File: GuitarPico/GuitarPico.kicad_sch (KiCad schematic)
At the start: 112 parts, among them J1 INPUT, J2 INPUT, J3 OUTPUT, J4 OUTPUT, J5 Barrel_Jack_Switch, J6 INPUT, J7 INPUT, J8 INPUT, J9 INPUT, Q1 2N3904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

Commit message: Before replacing with buttons
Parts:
- added C30: 100 pF, Capacitor_THT:C_Disc_D5.0mm_W2.5mm_P5.00mm, symbol Device:C_Small
- C12: value 330 nF -> 220 pF
- C13: value 2200 pF -> 220 pF
- R13, R14, R15: value 1k -> 10k
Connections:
- net CTRLIN: now also C30.1
- net GND: now also C30.2
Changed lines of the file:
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@@
   (junction (at 283.21 77.47) (diameter 0) (color 0 0 0 0)
   )
+  (junction (at 279.4 115.57) (diameter 0) (color 0 0 0 0)
+  )
   (junction (at 76.2 92.075) (diameter 0) (color 0 0 0 0)
   )
@@
     (stroke (width 0) (type default) (color 0 0 0 0))
   )
+  (wire (pts (xy 276.86 115.57) (xy 279.4 115.57))
+    (stroke (width 0) (type default) (color 0 0 0 0))
+  )
   (wire (pts (xy 110.49 103.505) (xy 101.6 103.505))
     (stroke (width 0) (type default) (color 0 0 0 0))
   )
+  (wire (pts (xy 279.4 115.57) (xy 279.4 114.935))
+    (stroke (width 0) (type default) (color 0 0 0 0))
+  )
   (wire (pts (xy 84.455 185.42) (xy 84.455 186.69))
     (stroke (width 0) (type default) (color 0 0 0 0))
@@
     (stroke (width 0) (type default) (color 0 0 0 0))
   )
+  (wire (pts (xy 279.4 116.205) (xy 279.4 115.57))
+    (stroke (width 0) (type default) (color 0 0 0 0))
+  )
   (wire (pts (xy 52.07 180.975) (xy 52.07 180.34))
     (stroke (width 0) (type default) (color 0 0 0 0))
@@
     (stroke (width 0) (type default) (color 0 0 0 0))
   )
+  (wire (pts (xy 276.86 132.08) (xy 276.86 133.985))
+    (stroke (width 0) (type default) (color 0 0 0 0))
+  )
   (wire (pts (xy 269.875 41.275) (xy 269.875 42.545))
     (stroke (width 0) (type default) (color 0 0 0 0))
@@
     (stroke (width 0) (type default) (color 0 0 0 0))
   )
+  (wire (pts (xy 276.86 115.57) (xy 276.86 127))
+    (stroke (width 0) (type default) (color 0 0 0 0))
+  )
   (wire (pts (xy 265.43 38.735) (xy 265.43 42.545))
     (stroke (width 0) (type default) (color 0 0 0 0))
@@
     )
   )
-  (global_label "CTRLIN" (shape input) (at 279.4 114.935 270) (fields_autoplaced)
+  (global_label "CTRLIN" (shape input) (at 279.4 116.205 270) (fields_autoplaced)
     (effects (font (size 1.27 1.27)) (justify right))
-    (property "Intersheet References" "${INTERSHEET_REFS}" (id 0) (at 279.4794 123.8191 90)
+    (property "Intersheet References" "${INTERSHEET_REFS}" (id 0) (at 279.4794 125.0891 90)
       (effects (font (size 1.27 1.27)) (justify right) hide)
     )
@@
     (pin "2")
   )
+  (symbol (lib_id "Device:C_Small") (at 276.86 129.54 0) (unit 1)
+    (in_bom yes) (on_board yes)
+    (property "Reference" "C30" (id 0) (at 280.67 130.81 0)
+      (effects (font (size 1.27 1.27)) (justify right))
+    )
+    (property "Value" "100 pF" (id 1) (at 284.48 127.635 0)
+      (effects (font (size 1.27 1.27)) (justify right))
+    )
+    (property "Footprint" "Capacitor_THT:C_Disc_D5.0mm_W2.5mm_P5.00mm" (id 2) (at 276.86 129.54 0)
+      (effects (font (size 1.27 1.27)) hide)
+    )
+    (property "Datasheet" "~" (id 3) (at 276.86 129.54 0)
+      (effects (font (size 1.27 1.27)) hide)
+    )
+    (pin "1")
+    (pin "2")
+  )
   (symbol (lib_id "Device:C_Small") (at 123.317 43.561 270) (unit 1)
     (in_bom yes) (on_board yes)
@@
       (effects (font (size 1.27 1.27)) (justify left))
     )
-    (property "Value" "1k" (id 1) (at 42.545 82.55 90)
+    (property "Value" "10k" (id 1) (at 42.545 82.55 90)
       (effects (font (size 1.27 1.27)) (justify left))
     )
@@
       (effects (font (size 1.27 1.27)) (justify left))
     )
-    (property "Value" "1k" (id 1) (at 54.61 82.55 90)
+    (property "Value" "10k" (id 1) (at 54.61 82.55 90)
       (effects (font (size 1.27 1.27)) (justify left))
     )
@@
       (effects (font (size 1.27 1.27)) (justify left))
     )
-    (property "Value" "330 nF" (id 1) (at 49.53 78.7462 0)
+    (property "Value" "220 pF" (id 1) (at 49.53 78.7462 0)
       (effects (font (size 1.27 1.27)) (justify left))
     )
@@
     (pin "2")
   )
+  (symbol (lib_id "power:GND") (at 276.86 133.985 0) (unit 1)
+    (in_bom yes) (on_board yes) (fields_autoplaced)
+    (property "Reference" "#PWR0154" (id 0) (at 276.86 140.335 0)
+      (effects (font (size 1.27 1.27)) hide)
+    )
+    (property "Value" "GND" (id 1) (at 276.86 138.43 0))
+    (property "Footprint" "" (id 2) (at 276.86 133.985 0)
+      (effects (font (size 1.27 1.27)) hide)
+    )
+    (property "Datasheet" "" (id 3) (at 276.86 133.985 0)
+      (effects (font (size 1.27 1.27)) hide)
+    )
+    (pin "1")
+  )
   (symbol (lib_id "power:+5V") (at 276.225 21.59 0) (unit 1)
     (in_bom yes) (on_board yes) (fields_autoplaced)
@@
       (effects (font (size 1.27 1.27)) (justify left))
     )
-    (property "Value" "1k" (id 1) (at 69.215 99.06 90)
+    (property "Value" "10k" (id 1) (at 69.215 99.06 90)
       (effects (font (size 1.27 1.27)) (justify left))
     )
@@
     (in_bom yes) (on_board yes)
     (property "Reference" "C13" (id 0) (at 67.945 88.9 90))
-    (property "Value" "2200 pF" (id 1) (at 67.945 95.25 90))
+    (property "Value" "220 pF" (id 1) (at 67.945 95.25 90))
     (property "Footprint" "Capacitor_THT:C_Disc_D5.0mm_W2.5mm_P5.00mm" (id 2) (at 67.945 92.075 0)
       (effects (font (size 1.27 1.27)) hide)
@@
       (reference "#PWR0153") (unit 1) (value "GND") (footprint "")
     )
+    (path "/c9b51cd9-edc6-4038-85ec-d1dec8977489"
+      (reference "#PWR0154") (unit 1) (value "GND") (footprint "")
+    )
     (path "/eeed5017-d7ea-4c03-bcf7-e3cc8a7830ea"
       (reference "Brd1") (unit 1) (value "SSD1306") (footprint "GuitarPico:128x64OLED")
@@
     )
     (path "/944a30cb-00bd-425f-b8d2-7613a7bc143d"
-      (reference "C12") (unit 1) (value "330 nF") (footprint "Capacitor_THT:C_Disc_D5.0mm_W2.5mm_P5.00mm")
+      (reference "C12") (unit 1) (value "220 pF") (footprint "Capacitor_THT:C_Disc_D5.0mm_W2.5mm_P5.00mm")
     )
     (path "/f9e582af-f7a7-46da-b838-4d87800ad119"
-      (reference "C13") (unit 1) (value "2200 pF") (footprint "Capacitor_THT:C_Disc_D5.0mm_W2.5mm_P5.00mm")
+      (reference "C13") (unit 1) (value "220 pF") (footprint "Capacitor_THT:C_Disc_D5.0mm_W2.5mm_P5.00mm")
     )
     (path "/7b62232e-dc1b-424a-bd96-df5531b112a2"
@@
       (reference "C29") (unit 1) (value "100 nF") (footprint "Capacitor_THT:C_Disc_D5.0mm_W2.5mm_P5.00mm")
     )
+    (path "/1c3bfbaf-43b7-4fed-90fb-53769c1c1fb4"
+      (reference "C30") (unit 1) (value "100 pF") (footprint "Capacitor_THT:C_Disc_D5.0mm_W2.5mm_P5.00mm")
+    )
     (path "/c47f2778-675e-4a19-8402-9385e9308b9c"
       (reference "D1") (unit 1) (value "1N5819") (footprint "Diode_THT:D_DO-41_SOD81_P7.62mm_Horizontal")
@@
     )
     (path "/497e8e16-db24-4b63-b1a9-654c978540b6"
-      (reference "R13") (unit 1) (value "1k") (footprint "Resistor_THT:R_Axial_DIN0207_L6.3mm_D2.5mm_P7.62mm_Horizontal")
+      (reference "R13") (unit 1) (value "10k") (footprint "Resistor_THT:R_Axial_DIN0207_L6.3mm_D2.5mm_P7.62mm_Horizontal")
     )
     (path "/8311fdd2-488f-44b2-97f8-bec3fa3e522a"
-      (reference "R14") (unit 1) (value "1k") (footprint "Resistor_THT:R_Axial_DIN0207_L6.3mm_D2.5mm_P7.62mm_Horizontal")
+      (reference "R14") (unit 1) (value "10k") (footprint "Resistor_THT:R_Axial_DIN0207_L6.3mm_D2.5mm_P7.62mm_Horizontal")
     )
     (path "/dee588ca-cd6f-49bd-8482-b92f631940ad"
-      (reference "R15") (unit 1) (value "1k") (footprint "Resistor_THT:R_Axial_DIN0207_L6.3mm_D2.5mm_P7.62mm_Horizontal")
+      (reference "R15") (unit 1) (value "10k") (footprint "Resistor_THT:R_Axial_DIN0207_L6.3mm_D2.5mm_P7.62mm_Horizontal")
     )
     (path "/f985247c-ef50-4b7d-a7ba-9d9ed0bb0d70"

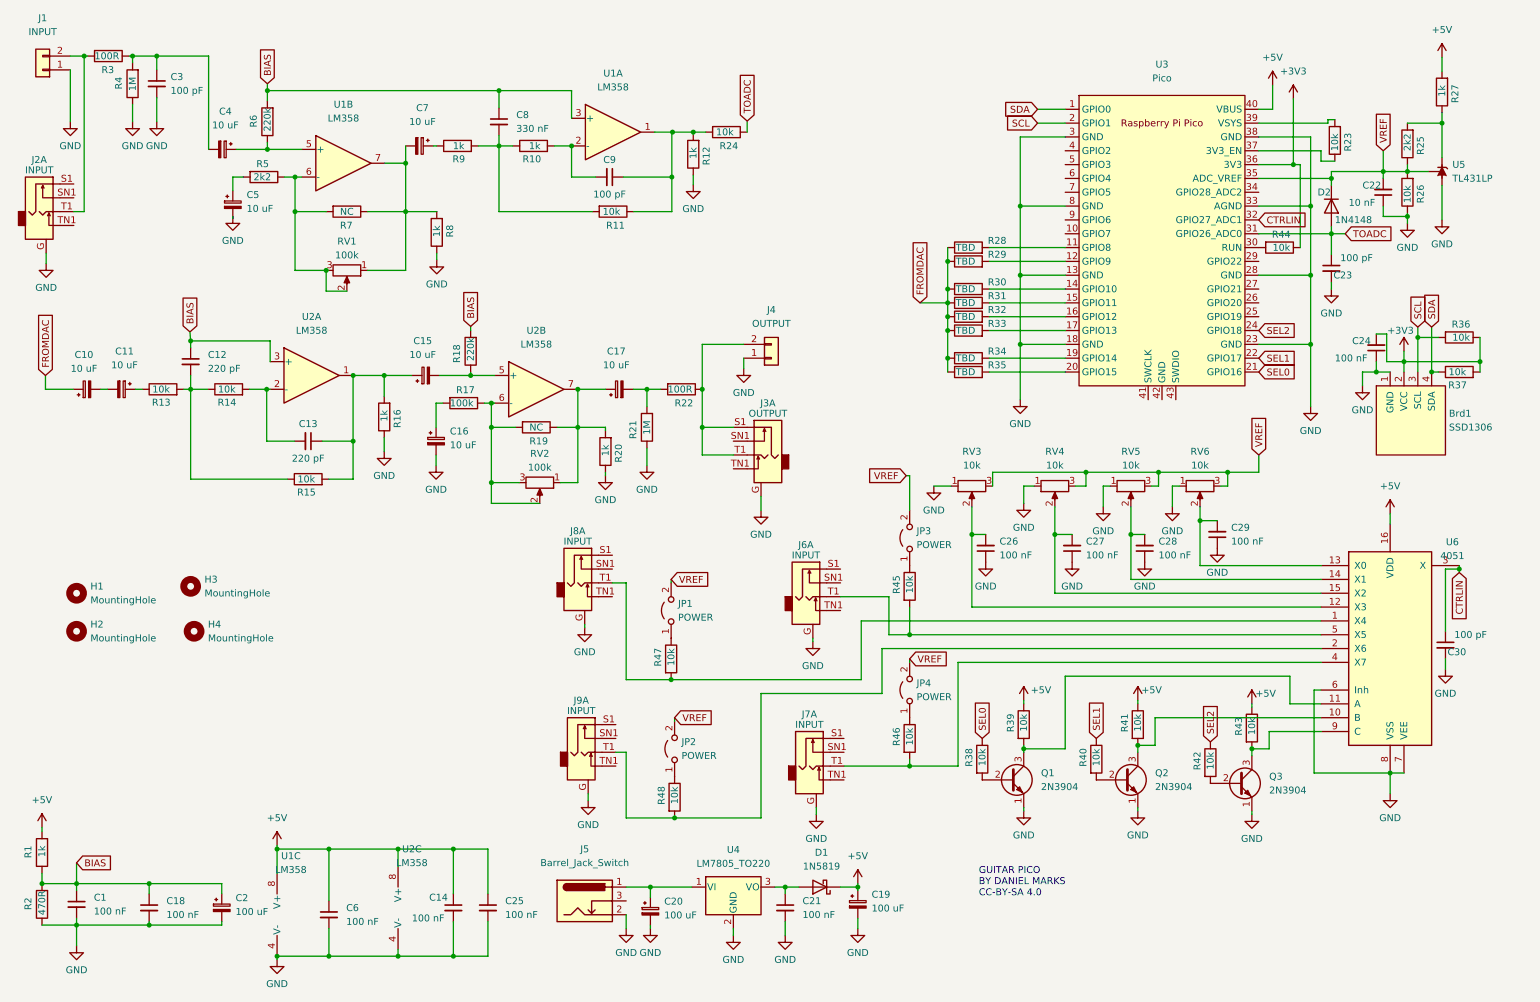
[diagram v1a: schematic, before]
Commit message: replaced with buttons
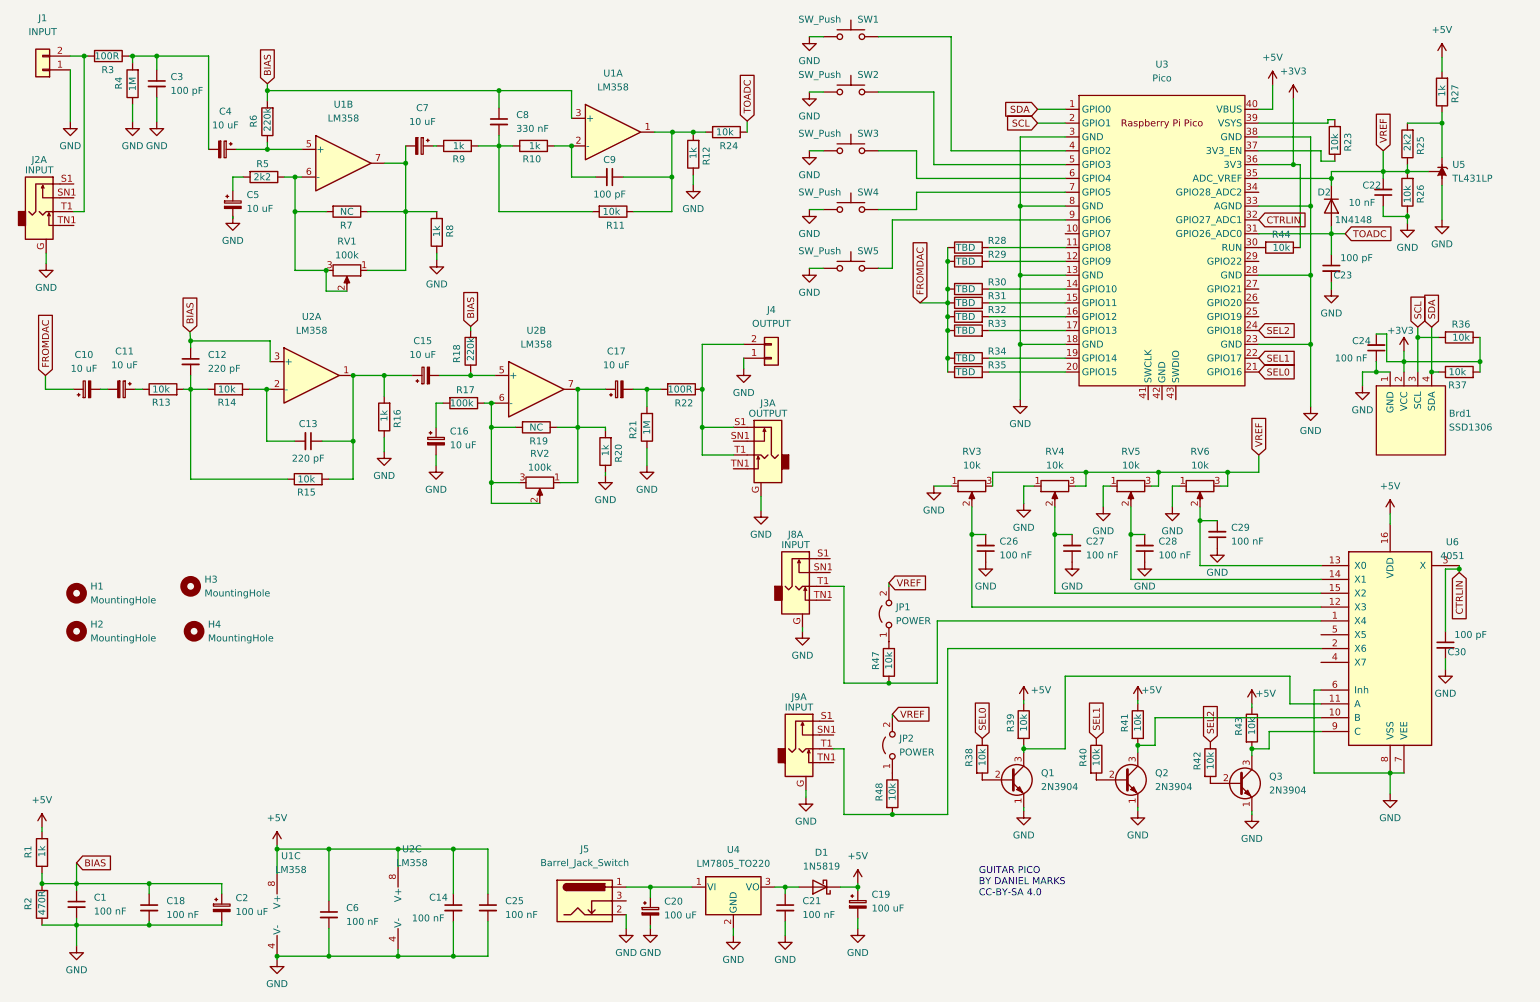
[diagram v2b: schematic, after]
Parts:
- removed J6, J7: INPUT, GuitarPico:PJ-3240-35mm-stereo, symbol Connector:AudioJack2_Dual_Ground_Switch
- removed JP3, JP4: POWER, Connector_PinHeader_2.54mm:PinHeader_1x02_P2.54mm_Vertical, symbol Jumper:Jumper_2_Open
- removed R45, R46: 10k, Resistor_THT:R_Axial_DIN0207_L6.3mm_D2.5mm_P7.62mm_Horizontal, symbol Device:R
- added SW1, SW2, SW3, SW4, SW5: SW_Push, Button_Switch_THT:SW_PUSH_6mm, symbol Switch:SW_Push
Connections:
- net GND: now also SW1.1, SW2.1, SW3.1, SW4.1, SW5.1
- net at U3.4 (GPIO2): now also SW1.2
- net at U3.5 (GPIO3): now also SW2.2
- net at U3.6 (GPIO4): now also SW3.2
- net at U3.7 (GPIO5): now also SW4.2
- net at U3.9 (GPIO6): now also SW5.2
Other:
- moved on the sheet: J8A, J9A, JP1, JP2, R47, R48

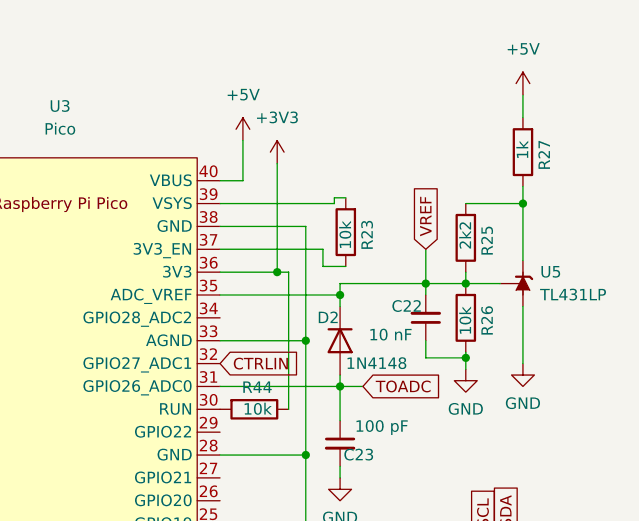
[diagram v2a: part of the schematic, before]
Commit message: Fixed TL431 wiring problem
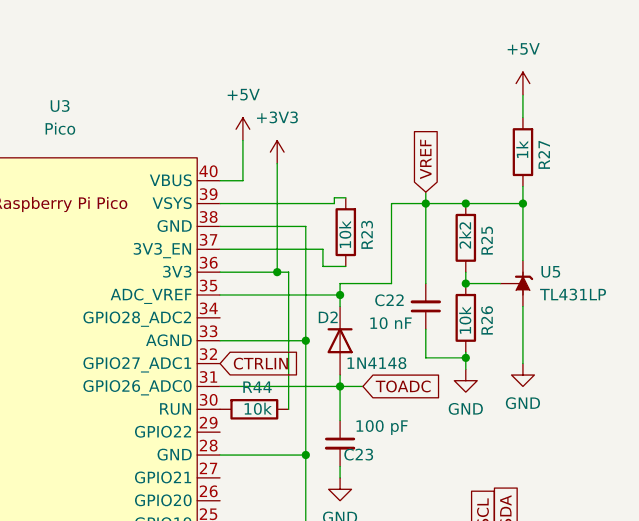
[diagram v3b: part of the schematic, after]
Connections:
- net VREF: now also R25.2, R27.1, U5.3 (K); no longer R25.1, R26.2, U5.1 (REF)
- new net: R25.1, R26.2, U5.1 (REF)
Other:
- moved on the sheet: C22
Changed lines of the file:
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@@
   (junction (at 224.155 97.79) (diameter 0) (color 0 0 0 0)
   )
+  (junction (at 265.43 33.655) (diameter 0) (color 0 0 0 0)
+  )
   (junction (at 241.3 148.59) (diameter 0) (color 0 0 0 0)
   )
@@
   (junction (at 189.865 109.22) (diameter 0) (color 0 0 0 0)
   )
+  (junction (at 269.875 33.655) (diameter 0) (color 0 0 0 0)
+  )
   (junction (at 185.42 69.215) (diameter 0) (color 0 0 0 0)
   )
@@
   (junction (at 252.095 61.595) (diameter 0) (color 0 0 0 0)
   )
-  (junction (at 265.43 42.545) (diameter 0) (color 0 0 0 0)
-  )
   (junction (at 94.615 167.005) (diameter 0) (color 0 0 0 0)
   )
@@
     (stroke (width 0) (type default) (color 0 0 0 0))
   )
-  (wire (pts (xy 25.4 179.705) (xy 25.4 180.975))
+  (wire (pts (xy 261.62 42.545) (xy 261.62 33.655))
     (stroke (width 0) (type default) (color 0 0 0 0))
   )
-  (wire (pts (xy 265.43 42.545) (xy 265.43 43.815))
+  (wire (pts (xy 25.4 179.705) (xy 25.4 180.975))
     (stroke (width 0) (type default) (color 0 0 0 0))
   )
@@
     (stroke (width 0) (type default) (color 0 0 0 0))
   )
+  (wire (pts (xy 265.43 32.385) (xy 265.43 33.655))
+    (stroke (width 0) (type default) (color 0 0 0 0))
+  )
   (wire (pts (xy 269.875 42.545) (xy 273.685 42.545))
     (stroke (width 0) (type default) (color 0 0 0 0))
@@
     (stroke (width 0) (type default) (color 0 0 0 0))
   )
-  (wire (pts (xy 265.43 48.895) (xy 265.43 50.8))
+  (wire (pts (xy 265.43 47.625) (xy 265.43 50.8))
     (stroke (width 0) (type default) (color 0 0 0 0))
   )
@@
     (stroke (width 0) (type default) (color 0 0 0 0))
   )
-  (wire (pts (xy 265.43 42.545) (xy 269.875 42.545))
-    (stroke (width 0) (type default) (color 0 0 0 0))
-  )
   (wire (pts (xy 130.175 82.55) (xy 132.715 82.55))
     (stroke (width 0) (type default) (color 0 0 0 0))
@@
     (stroke (width 0) (type default) (color 0 0 0 0))
   )
-  (wire (pts (xy 255.905 42.545) (xy 265.43 42.545))
+  (wire (pts (xy 255.905 42.545) (xy 261.62 42.545))
     (stroke (width 0) (type default) (color 0 0 0 0))
   )
@@
     (stroke (width 0) (type default) (color 0 0 0 0))
   )
-  (wire (pts (xy 265.43 38.735) (xy 265.43 42.545))
-    (stroke (width 0) (type default) (color 0 0 0 0))
-  )
   (wire (pts (xy 235.585 100.33) (xy 236.855 100.33))
     (stroke (width 0) (type default) (color 0 0 0 0))
@@
     (stroke (width 0) (type default) (color 0 0 0 0))
   )
+  (wire (pts (xy 265.43 33.655) (xy 269.875 33.655))
+    (stroke (width 0) (type default) (color 0 0 0 0))
+  )
   (wire (pts (xy 185.42 64.135) (xy 185.42 66.675))
     (stroke (width 0) (type default) (color 0 0 0 0))
@@
     (stroke (width 0) (type default) (color 0 0 0 0))
   )
+  (wire (pts (xy 261.62 33.655) (xy 265.43 33.655))
+    (stroke (width 0) (type default) (color 0 0 0 0))
+  )
   (wire (pts (xy 244.475 148.59) (xy 244.475 145.415))
     (stroke (width 0) (type default) (color 0 0 0 0))
@@
     (stroke (width 0) (type default) (color 0 0 0 0))
   )
+  (wire (pts (xy 265.43 33.655) (xy 265.43 42.545))
+    (stroke (width 0) (type default) (color 0 0 0 0))
+  )
   (wire (pts (xy 271.78 73.025) (xy 275.59 73.025))
     (stroke (width 0) (type default) (color 0 0 0 0))
@@
     )
   )
-  (global_label "VREF" (shape input) (at 265.43 38.735 90) (fields_autoplaced)
+  (global_label "VREF" (shape input) (at 265.43 32.385 90) (fields_autoplaced)
     (effects (font (size 1.27 1.27)) (justify left))
-    (property "Intersheet References" "${INTERSHEET_REFS}" (id 0) (at 265.3506 31.7257 90)
+    (property "Intersheet References" "${INTERSHEET_REFS}" (id 0) (at 265.3506 25.3757 90)
       (effects (font (size 1.27 1.27)) (justify left) hide)
     )
@@
     (pin "2")
   )
-  (symbol (lib_id "Device:C_Small") (at 265.43 46.355 180) (unit 1)
+  (symbol (lib_id "Device:C_Small") (at 265.43 45.085 180) (unit 1)
     (in_bom yes) (on_board yes)
-    (property "Reference" "C22" (id 0) (at 261.62 45.085 0)
+    (property "Reference" "C22" (id 0) (at 259.715 44.45 0)
       (effects (font (size 1.27 1.27)) (justify right))
     )
-    (property "Value" "10 nF" (id 1) (at 259.08 48.26 0)
+    (property "Value" "10 nF" (id 1) (at 259.08 46.99 0)
       (effects (font (size 1.27 1.27)) (justify right))
     )
-    (property "Footprint" "Capacitor_THT:C_Disc_D5.0mm_W2.5mm_P5.00mm" (id 2) (at 265.43 46.355 0)
+    (property "Footprint" "Capacitor_THT:C_Disc_D5.0mm_W2.5mm_P5.00mm" (id 2) (at 265.43 45.085 0)
       (effects (font (size 1.27 1.27)) hide)
     )
-    (property "Datasheet" "~" (id 3) (at 265.43 46.355 0)
+    (property "Datasheet" "~" (id 3) (at 265.43 45.085 0)
       (effects (font (size 1.27 1.27)) hide)
     )
